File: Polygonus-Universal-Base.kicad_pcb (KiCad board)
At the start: 2 copper layers, 160 x 118 mm, 70 parts, among them J1 Conn_02x04_Top_Bottom, J4 Polygonus_Plugs, J5 Conn_02x04_Top_Bottom, Q1 NGD8201AN, Q2 NGD8201AN, Q3 NGD8201AN, Q4 NGD8201AN, Q5 NGD8201AN, Q6 NGD8201AN, Q7 NGD8201AN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

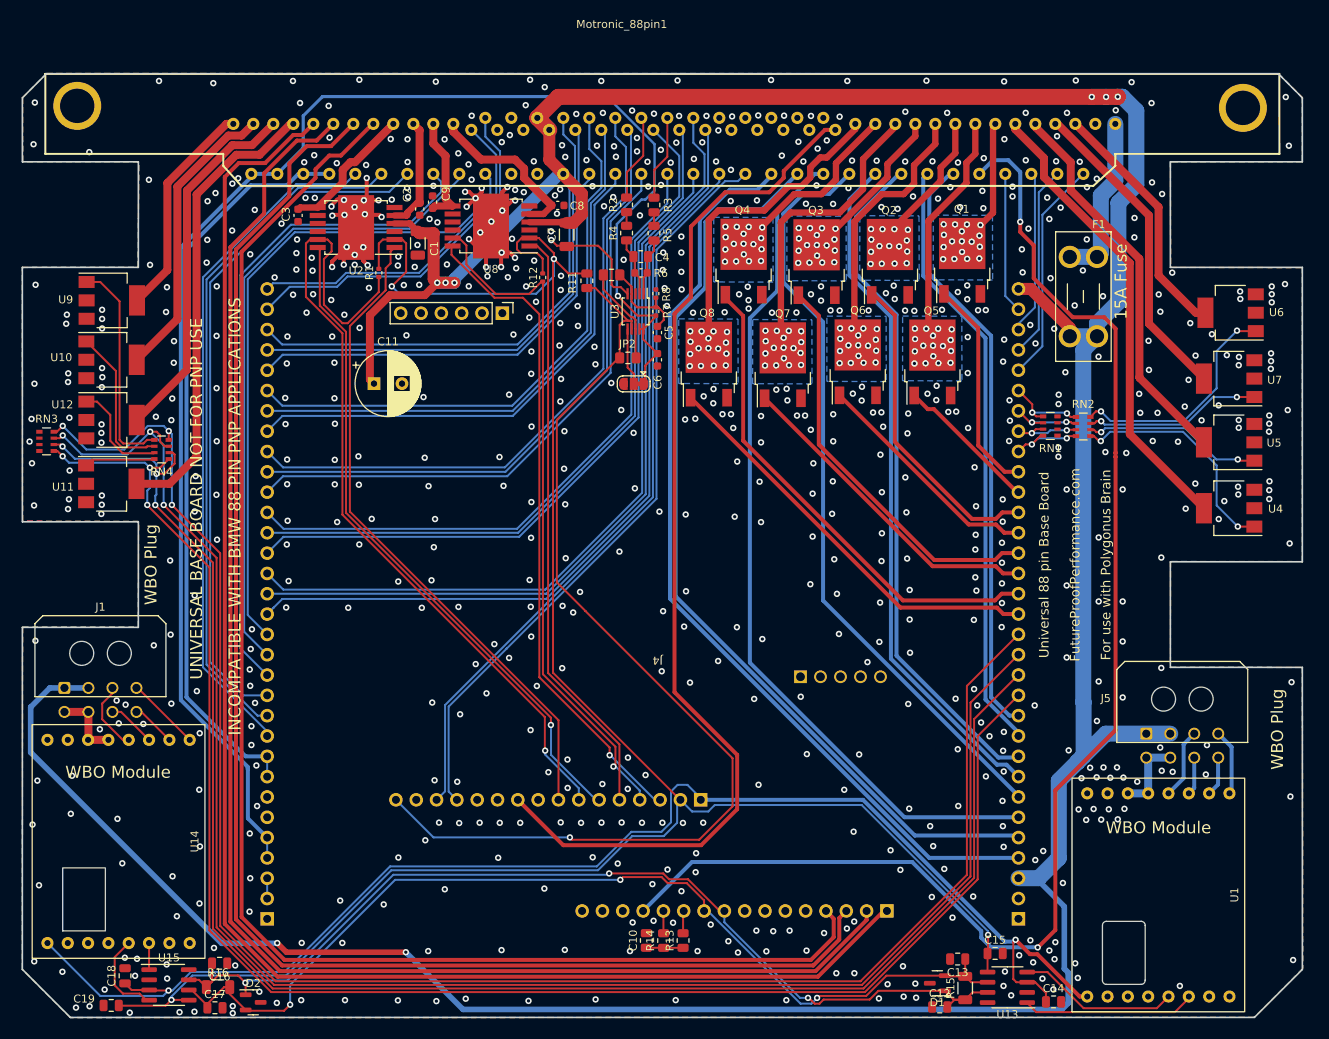
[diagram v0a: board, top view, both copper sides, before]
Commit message: Modified IGBTs and routed smart coils
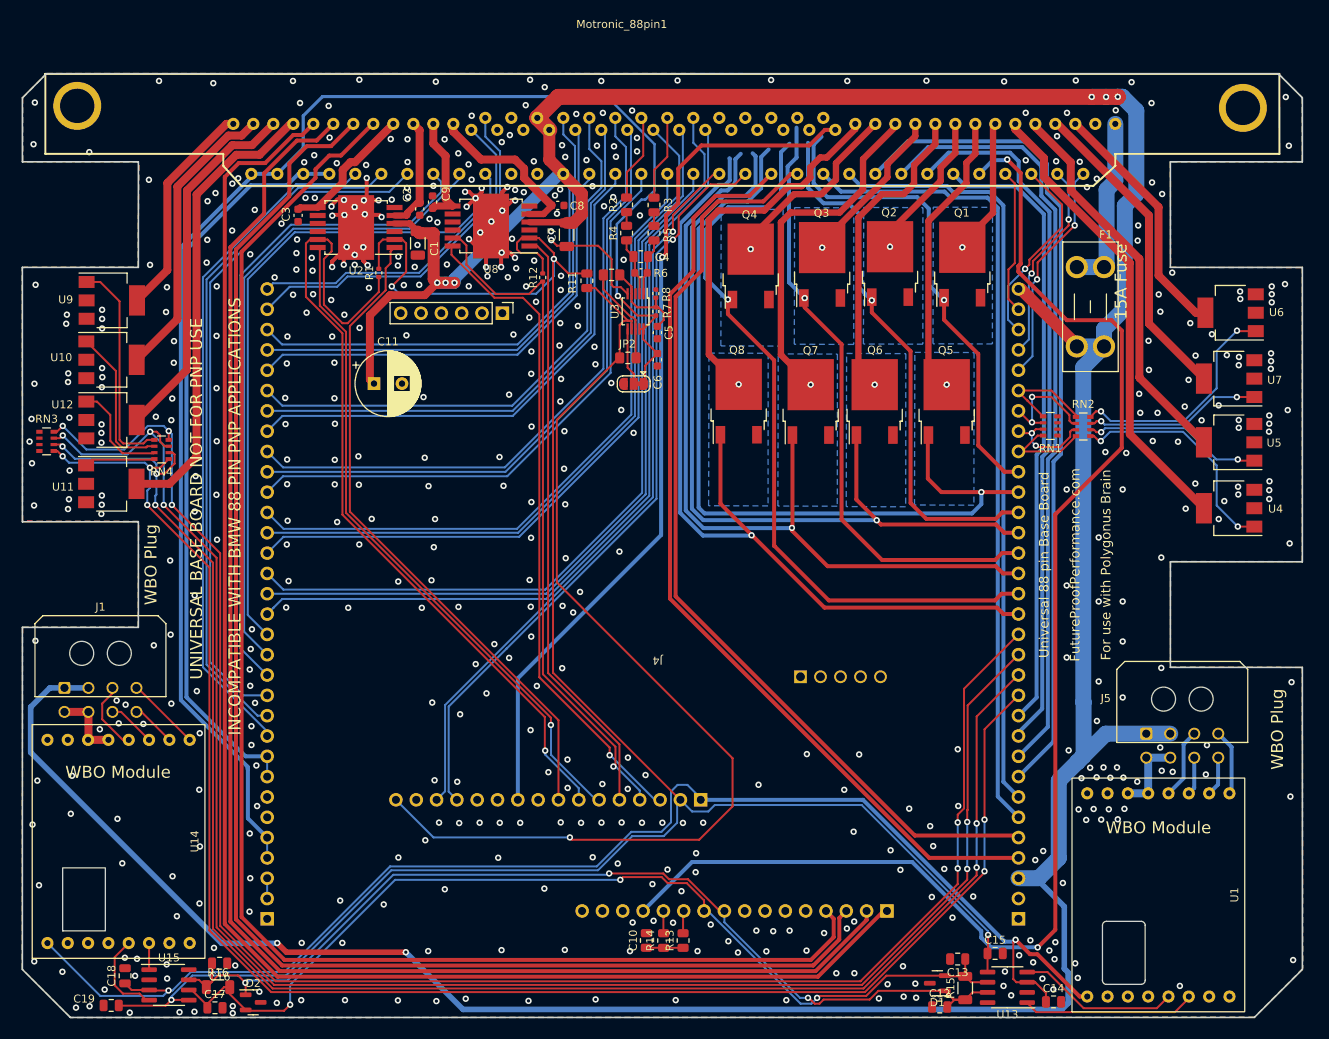
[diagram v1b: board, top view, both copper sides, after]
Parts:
- moved Q8 5.95 mm to (146.7, 67.3)
- moved Q7 5.77 mm to (155.7, 67.3)
- moved Q6 5.40 mm to (163.7, 67.3)
- moved Q5 5.26 mm to (172.7, 67.3)
- moved F1 1.55 mm to (192.4, 50.5)
- moved Q4 1.07 mm to (148.2, 50.4)
- moved Q3 0.78 mm to (157.1, 50.2)
- moved Q1 0.48 mm to (174.7, 50.2)
- moved Q2 0.28 mm to (165.6, 50.1)
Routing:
- net /IGN2: track 18.0 -> 105.1 mm, vias 0 -> 1
- net /IGN4: track 29.5 -> 103.3 mm, vias 0 -> 1
- net /IGN6: track 40.8 -> 104.6 mm, vias 0 -> 1
- net /IGN8: track 52.2 -> 109.1 mm, vias 0 -> 1
- net /IGN1: track 27.1 -> 60.8 mm, vias 0 -> 1
- net /IGN7: track 62.2 -> 95.4 mm, vias 0 -> 1
- net /IGN3: track 39.5 -> 67.2 mm, vias 0 -> 1
- net /IGN5: track 51.0 -> 76.9 mm, vias 0 -> 1
- net /12V_KEY: track 132.1 -> 108.8 mm, vias 0 -> 1
- net /LS5: track 86.1 -> 103.8 mm
- net /LS7: track 75.4 -> 88.0 mm
- net /LS6: track 85.4 -> 96.3 mm
- net /LS3: track 107.1 -> 100.8 mm
- net /IGBT8: track 40.5 -> 46.7 mm, vias 16 -> 1
- net /IGBT6: track 37.6 -> 43.6 mm, vias 17 -> 1
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
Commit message: updated and fixed, check JLC exports
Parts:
- C2, C3, C4, C5, C8, C9: footprint Capacitor_SMD:C_0603_1608Metric -> Capacitor_SMD:C_0805_2012Metric
- C6: footprint Capacitor_SMD:C_0603_1608Metric -> Capacitor_SMD:C_0805_2012Metric_Pad1.18x1.45mm_HandSolder
- R1, R12, R7, R8: footprint Resistor_SMD:R_0402_1005Metric -> Resistor_SMD:R_0805_2012Metric
- moved C6 2.49 mm to (136.6, 64.6)
- moved C5 2.15 mm to (136.8, 60.9)
- moved R7 1.30 mm to (136.8, 57.3)
- moved R1 0.99 mm to (101.3, 52.2)
- moved JP2 0.76 mm to (132.8, 65.1)
- moved R12 0.55 mm to (121.7, 52.1)
- moved R8 0.43 mm to (136.8, 53.8)
- moved C9 0.29 mm to (108.6, 42.2)
- moved C1 0.29 mm to (106.6, 47.9)
- moved C2 0.28 mm to (106.6, 43.5)
- moved R6 0.27 mm to (134.5, 49.0)
- moved C4 0.23 mm to (134.5, 51.0)
- moved R5 0.14 mm to (136.2, 46.2)
- moved R4 0.09 mm to (132.7, 46.2)
- moved R3 0.09 mm to (136.1, 42.7)
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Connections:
- Motronic_88pin1 pad 17: unconnected-(Motronic_88pin1-Pad17) -> /IGN8
- Motronic_88pin1 pad 18: unconnected-(Motronic_88pin1-Pad18) -> /IGN4
- Motronic_88pin1 pad 19: unconnected-(Motronic_88pin1-Pad19) -> /IGN7
- Motronic_88pin1 pad 20: unconnected-(Motronic_88pin1-Pad20) -> /IGN3
- Motronic_88pin1 pad 45: unconnected-(Motronic_88pin1-Pad45) -> /IGN6
- Motronic_88pin1 pad 46: unconnected-(Motronic_88pin1-Pad46) -> /IGN2
- Motronic_88pin1 pad 47: unconnected-(Motronic_88pin1-Pad47) -> /IGN5
- Motronic_88pin1 pad 48: unconnected-(Motronic_88pin1-Pad48) -> /IGN1
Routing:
- net GND: track 61.8 -> 81.8 mm, vias 518 -> 726
- net /IGN6: track 104.6 -> 109.2 mm
- net /IGN4: track 103.3 -> 107.2 mm
- net /IGN2: track 105.1 -> 109.0 mm
- net /IGN8: track 109.1 -> 112.6 mm
- net /IGN1: track 60.8 -> 63.3 mm
- net Net-(C5-Pad1): track 11.8 -> 13.9 mm
- net /IGN3: track 67.2 -> 68.9 mm
- net /ETB2_DIS: track 106.6 -> 105.2 mm
- net /IGN5: track 76.9 -> 78.4 mm
- net /ETB1_DIS: track 86.4 -> 85.2 mm
- net /LS10: track 11.5 -> 12.7 mm
- net /IGN12: track 207.1 -> 208.0 mm
- net /+3V3: track 264.4 -> 265.0 mm
- net /IGBT8: track 46.7 -> 47.1 mm, vias 1 -> 9
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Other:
- outline, holes or cut-outs redrawn
- board text added: "IGBT 1"
- board text added: "IGBT 2"
- board text added: "IGBT 3"
- board text added: "IGBT 4"
- board text added: "IGBT 5"
- board text added: "IGBT 6"
- board text added: "IGBT 7"
- board text added: "IGBT 8"

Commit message: Fixed 12V_RAW and added grounds for sensors
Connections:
- Motronic_88pin1 pad 36: unconnected-(Motronic_88pin1-Pad36) -> GND
- Motronic_88pin1 pad 44: unconnected-(Motronic_88pin1-Pad44) -> GND
- Motronic_88pin1 pad 66: unconnected-(Motronic_88pin1-Pad66) -> GND
- Motronic_88pin1 pad 67: unconnected-(Motronic_88pin1-Pad67) -> GND
- Motronic_88pin1 pad 8: unconnected-(Motronic_88pin1-Pad8) -> GND
- Motronic_88pin1 pad 9: unconnected-(Motronic_88pin1-Pad9) -> GND

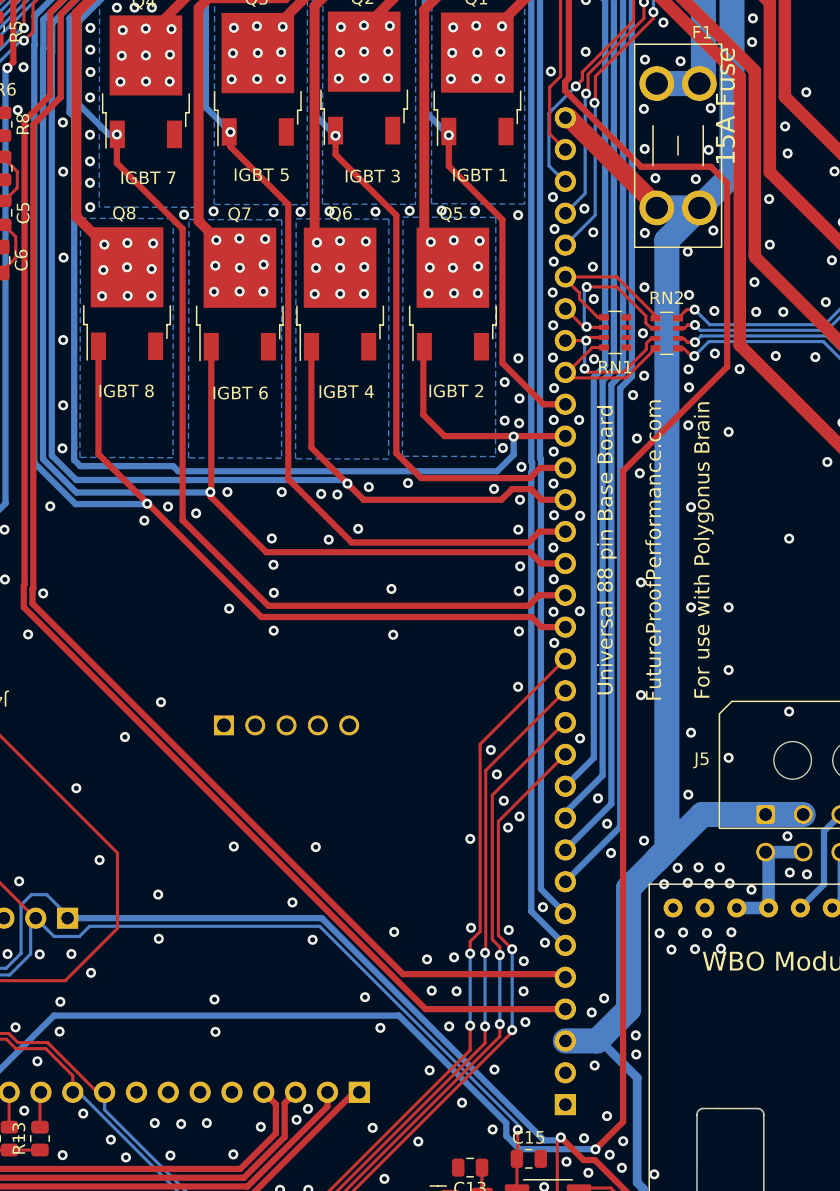
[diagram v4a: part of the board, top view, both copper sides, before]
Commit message: convert to kicad7, add jumpers for direct drive igbt output
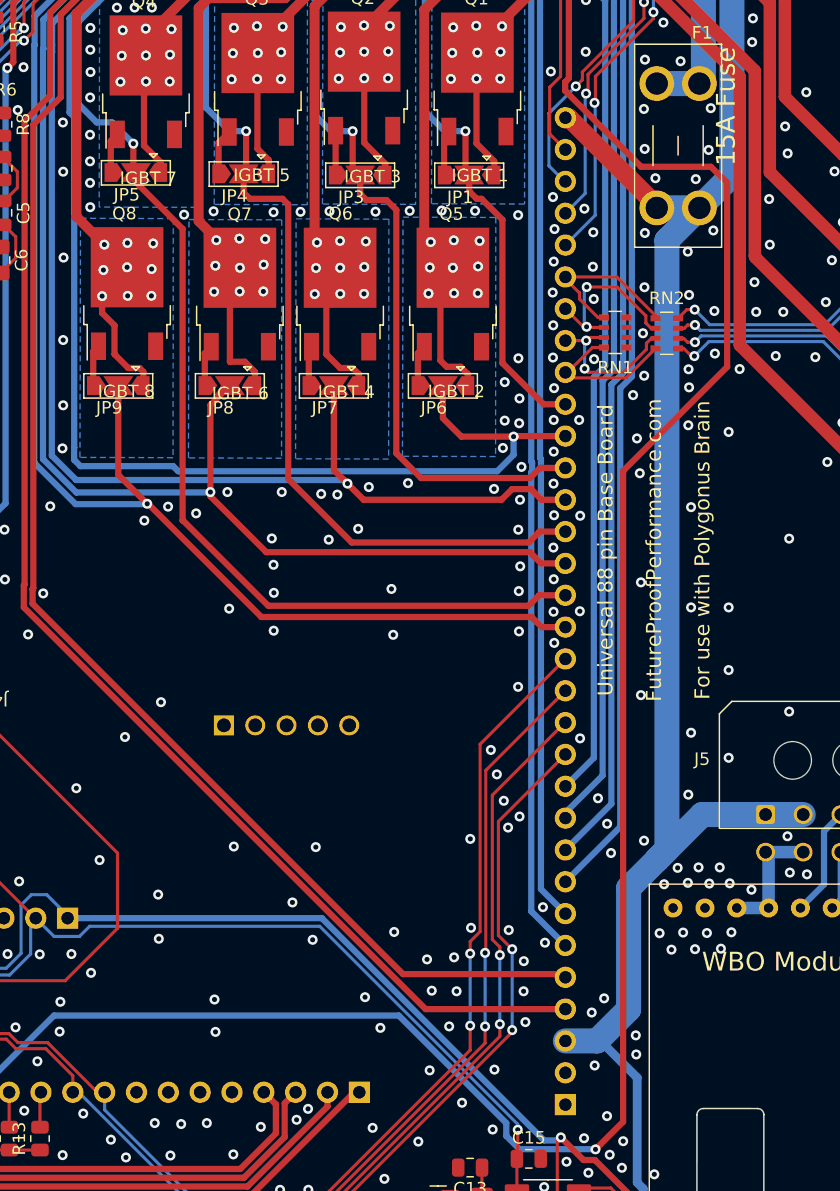
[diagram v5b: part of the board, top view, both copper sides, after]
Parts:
- added JP1: Jumper_3_Open, Jumper:SolderJumper-3_P2.0mm_Open_TrianglePad1.0x1.5mm, F.Cu at (174.0, 57.8)
- added JP3: Jumper_3_Open, Jumper:SolderJumper-3_P2.0mm_Open_TrianglePad1.0x1.5mm, F.Cu at (165.3, 57.8)
- added JP4: Jumper_3_Open, Jumper:SolderJumper-3_P2.0mm_Open_TrianglePad1.0x1.5mm, F.Cu at (156.0, 57.7)
- added JP5: Jumper_3_Open, Jumper:SolderJumper-3_P2.0mm_Open_TrianglePad1.0x1.5mm, F.Cu at (147.4, 57.6)
- added JP6: Jumper_3_Open, Jumper:SolderJumper-3_P2.0mm_Open_TrianglePad1.0x1.5mm, F.Cu at (171.9, 74.6)
- added JP7: Jumper_3_Open, Jumper:SolderJumper-3_P2.0mm_Open_TrianglePad1.0x1.5mm, F.Cu at (163.2, 74.6)
- added JP8: Jumper_3_Open, Jumper:SolderJumper-3_P2.0mm_Open_TrianglePad1.0x1.5mm, F.Cu at (154.9, 74.6)
- added JP9: Jumper_3_Open, Jumper:SolderJumper-3_P2.0mm_Open_TrianglePad1.0x1.5mm, F.Cu at (146.0, 74.6)
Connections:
- Q1 pad 1: /IGN1 -> Net-(JP1-B)
- Q2 pad 1: /IGN3 -> Net-(JP3-B)
- Q3 pad 1: /IGN5 -> Net-(JP4-B)
- Q4 pad 1: /IGN7 -> Net-(JP5-B)
- Q5 pad 1: /IGN2 -> Net-(JP6-B)
- Q6 pad 1: /IGN4 -> Net-(JP7-B)
- Q7 pad 1: /IGN6 -> Net-(JP8-B)
- Q8 pad 1: /IGN8 -> Net-(JP9-B)
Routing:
- net /IGBT4: track 39.3 -> 50.8 mm
- net /IGBT2: track 36.0 -> 47.3 mm
- net /IGBT6: track 43.3 -> 54.6 mm
- net /IGBT8: track 47.1 -> 56.1 mm
- net /IGBT3: track 18.7 -> 27.2 mm
- net /IGBT1: track 17.2 -> 25.4 mm
- net /IGBT5: track 20.3 -> 28.2 mm
- net /IGBT7: track 24.1 -> 32.0 mm
- net /IGN2: track 109.0 -> 104.5 mm
- net Net-(JP1-B): track 0.00 -> 3.92 mm
- net /IGN4: track 107.2 -> 103.3 mm
- net Net-(JP4-B): track 0.00 -> 3.78 mm
- net /IGN8: track 112.6 -> 108.8 mm
- net Net-(JP3-B): track 0.00 -> 3.55 mm
- net Net-(JP6-B): track 0.00 -> 3.42 mm
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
